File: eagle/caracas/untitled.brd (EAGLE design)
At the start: 110.2 x 53.3 mm, 26 parts, among them IC1 4027N, Q1 IRLZ44Z, X1 22-23-2021, X2 22-23-2021, X3 22-23-2041, X4 22-23-2041, X5 22-23-2021, X6 22-23-2021

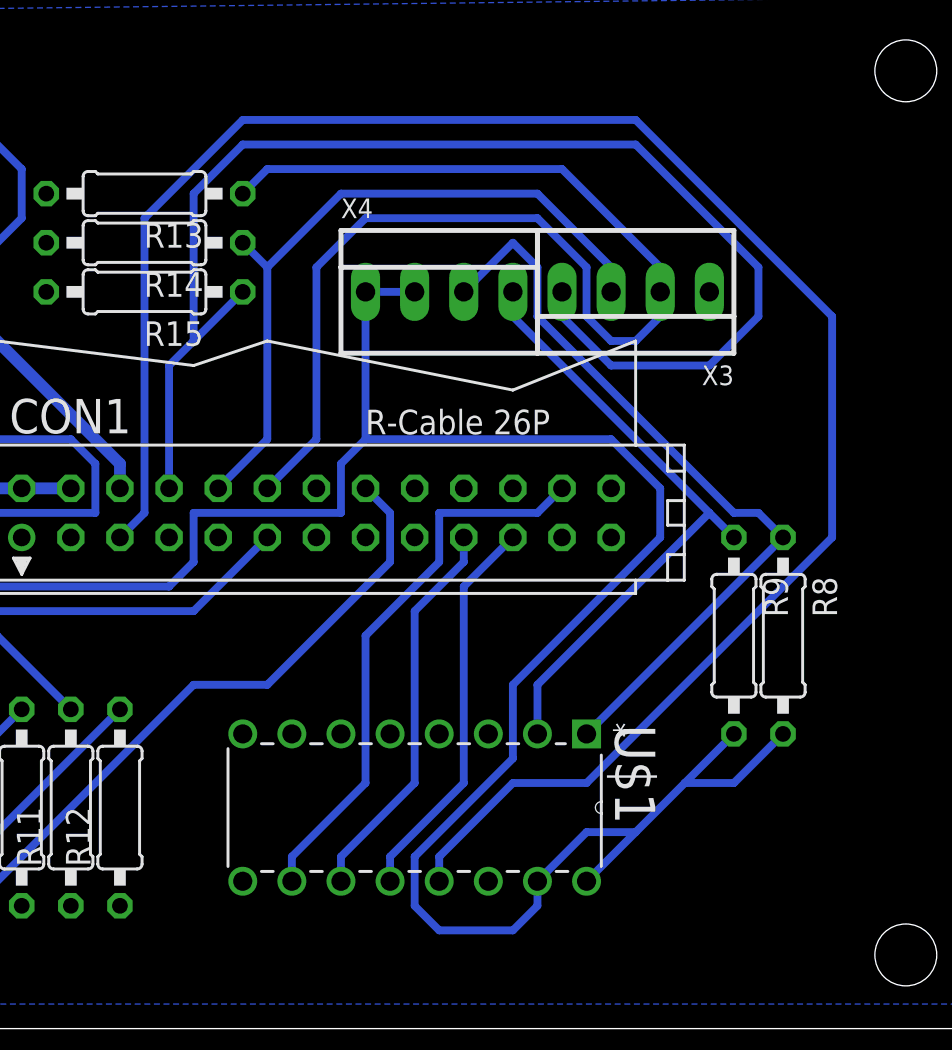
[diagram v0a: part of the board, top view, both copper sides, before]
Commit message: SPI clock in on pin 23, not pin 5
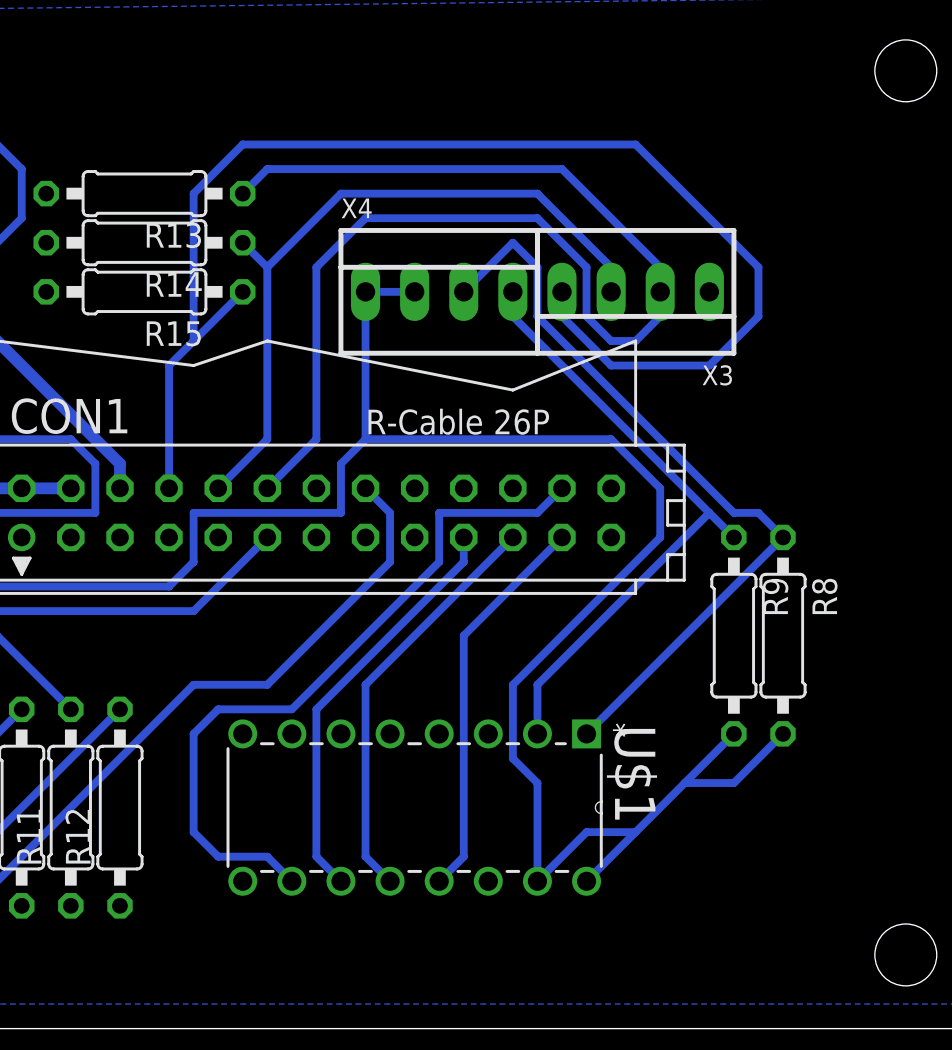
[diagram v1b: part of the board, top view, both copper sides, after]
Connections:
- net N$3: now also CON1.23; no longer CON1.5
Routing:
- net N$3: track 98.8 -> 20.4 mm
- net +3.3V: track 144.9 -> 133.4 mm
- net N$6: track 29.1 -> 37.0 mm
- net N$4: track 20.4 -> 21.5 mm
- net N$5: track 20.4 -> 21.5 mm
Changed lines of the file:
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@@
 <wire x1="59.69" y1="22.86" x2="68.58" y2="22.86" width="0.4064" layer="16"/>
 <wire x1="57.15" y1="25.4" x2="59.69" y2="22.86" width="0.4064" layer="16"/>
-<wire x1="87.63" y1="6.35" x2="87.63" y2="7.62" width="0.4064" layer="16"/>
-<wire x1="86.36" y1="5.08" x2="87.63" y2="6.35" width="0.4064" layer="16"/>
-<wire x1="82.55" y1="5.08" x2="86.36" y2="5.08" width="0.4064" layer="16"/>
-<wire x1="81.28" y1="6.35" x2="82.55" y2="5.08" width="0.4064" layer="16"/>
-<wire x1="81.28" y1="8.89" x2="81.28" y2="6.35" width="0.4064" layer="16"/>
-<wire x1="86.36" y1="13.97" x2="81.28" y2="8.89" width="0.4064" layer="16"/>
 <wire x1="86.36" y1="17.78" x2="86.36" y2="13.97" width="0.4064" layer="16"/>
 <wire x1="93.98" y1="25.4" x2="86.36" y2="17.78" width="0.4064" layer="16"/>
@@
 <wire x1="91.44" y1="30.48" x2="93.98" y2="27.94" width="0.4064" layer="16"/>
 <wire x1="78.74" y1="30.48" x2="91.44" y2="30.48" width="0.4064" layer="16"/>
+<wire x1="86.36" y1="13.97" x2="87.63" y2="12.7" width="0.4064" layer="16"/>
+<wire x1="87.63" y1="12.7" x2="87.63" y2="7.62" width="0.4064" layer="16"/>
 </signal>
 <signal name="+3.3V1">
@@
 <wire x1="57.15" y1="41.91" x2="55.88" y2="41.91" width="0.6096" layer="16"/>
 </signal>
-<signal name="N$3">
-<contactref element="CON1" pad="5"/>
-<contactref element="U$1" pad="13"/>
-<wire x1="67.31" y1="26.67" x2="66.04" y2="25.4" width="0.4064" layer="16"/>
-<wire x1="67.31" y1="41.91" x2="67.31" y2="26.67" width="0.4064" layer="16"/>
-<wire x1="72.39" y1="46.99" x2="67.31" y2="41.91" width="0.4064" layer="16"/>
-<wire x1="92.71" y1="46.99" x2="72.39" y2="46.99" width="0.4064" layer="16"/>
-<wire x1="102.87" y1="36.83" x2="92.71" y2="46.99" width="0.4064" layer="16"/>
-<wire x1="82.55" y1="7.62" x2="82.55" y2="8.89" width="0.4064" layer="16"/>
-<wire x1="82.55" y1="8.89" x2="86.36" y2="12.7" width="0.4064" layer="16"/>
-<wire x1="86.36" y1="12.7" x2="90.17" y2="12.7" width="0.4064" layer="16"/>
-<wire x1="102.87" y1="25.4" x2="102.87" y2="36.83" width="0.4064" layer="16"/>
-<wire x1="90.17" y1="12.7" x2="102.87" y2="25.4" width="0.4064" layer="16"/>
-</signal>
 <signal name="N$4">
 <contactref element="CON1" pad="21"/>
 <contactref element="U$1" pad="12"/>
-<wire x1="83.82" y1="22.86" x2="86.36" y2="25.4" width="0.4064" layer="16"/>
-<wire x1="83.82" y1="12.7" x2="83.82" y2="22.86" width="0.4064" layer="16"/>
-<wire x1="80.01" y1="8.89" x2="83.82" y2="12.7" width="0.4064" layer="16"/>
-<wire x1="80.01" y1="7.62" x2="80.01" y2="8.89" width="0.4064" layer="16"/>
+<wire x1="86.36" y1="25.4" x2="78.74" y2="17.78" width="0.4064" layer="16"/>
+<wire x1="78.74" y1="17.78" x2="78.74" y2="8.89" width="0.4064" layer="16"/>
+<wire x1="78.74" y1="8.89" x2="80.01" y2="7.62" width="0.4064" layer="16"/>
 </signal>
 <signal name="N$5">
@@
 <contactref element="U$1" pad="11"/>
 <wire x1="83.82" y1="24.13" x2="83.82" y2="25.4" width="0.4064" layer="16"/>
-<wire x1="81.28" y1="21.59" x2="83.82" y2="24.13" width="0.4064" layer="16"/>
-<wire x1="81.28" y1="12.7" x2="81.28" y2="21.59" width="0.4064" layer="16"/>
-<wire x1="77.47" y1="8.89" x2="81.28" y2="12.7" width="0.4064" layer="16"/>
-<wire x1="77.47" y1="7.62" x2="77.47" y2="8.89" width="0.4064" layer="16"/>
+<wire x1="83.82" y1="24.13" x2="76.2" y2="16.51" width="0.4064" layer="16"/>
+<wire x1="76.2" y1="16.51" x2="76.2" y2="8.89" width="0.4064" layer="16"/>
+<wire x1="76.2" y1="8.89" x2="77.47" y2="7.62" width="0.4064" layer="16"/>
 </signal>
 <signal name="N$6">
@@
 <wire x1="82.55" y1="26.67" x2="87.63" y2="26.67" width="0.4064" layer="16"/>
 <wire x1="82.55" y1="24.13" x2="82.55" y2="26.67" width="0.4064" layer="16"/>
-<wire x1="78.74" y1="20.32" x2="82.55" y2="24.13" width="0.4064" layer="16"/>
-<wire x1="78.74" y1="12.7" x2="78.74" y2="20.32" width="0.4064" layer="16"/>
-<wire x1="74.93" y1="8.89" x2="78.74" y2="12.7" width="0.4064" layer="16"/>
-<wire x1="74.93" y1="7.62" x2="74.93" y2="8.89" width="0.4064" layer="16"/>
+<wire x1="74.93" y1="7.62" x2="74.93" y2="8.89" width="0" layer="19" extent="1-16"/>
+<wire x1="82.55" y1="24.13" x2="74.93" y2="16.51" width="0.4064" layer="16"/>
+<wire x1="74.93" y1="16.51" x2="71.12" y2="16.51" width="0.4064" layer="16"/>
+<wire x1="71.12" y1="16.51" x2="69.85" y2="15.24" width="0.4064" layer="16"/>
+<wire x1="69.85" y1="15.24" x2="69.85" y2="10.16" width="0.4064" layer="16"/>
+<wire x1="69.85" y1="10.16" x2="71.12" y2="8.89" width="0.4064" layer="16"/>
+<wire x1="71.12" y1="8.89" x2="73.66" y2="8.89" width="0.4064" layer="16"/>
+<wire x1="73.66" y1="8.89" x2="74.93" y2="7.62" width="0.4064" layer="16"/>
 </signal>
 <signal name="N$9">
@@
 <wire x1="53.34" y1="22.86" x2="52.07" y2="22.86" width="0.4064" layer="16"/>
 </signal>
+<signal name="N$3">
+<contactref element="U$1" pad="13"/>
+<contactref element="CON1" pad="23"/>
+<wire x1="88.9" y1="25.4" x2="83.82" y2="20.32" width="0.4064" layer="16"/>
+<wire x1="83.82" y1="20.32" x2="83.82" y2="8.89" width="0.4064" layer="16"/>
+<wire x1="83.82" y1="8.89" x2="82.55" y2="7.62" width="0.4064" layer="16"/>
+</signal>
 </signals>

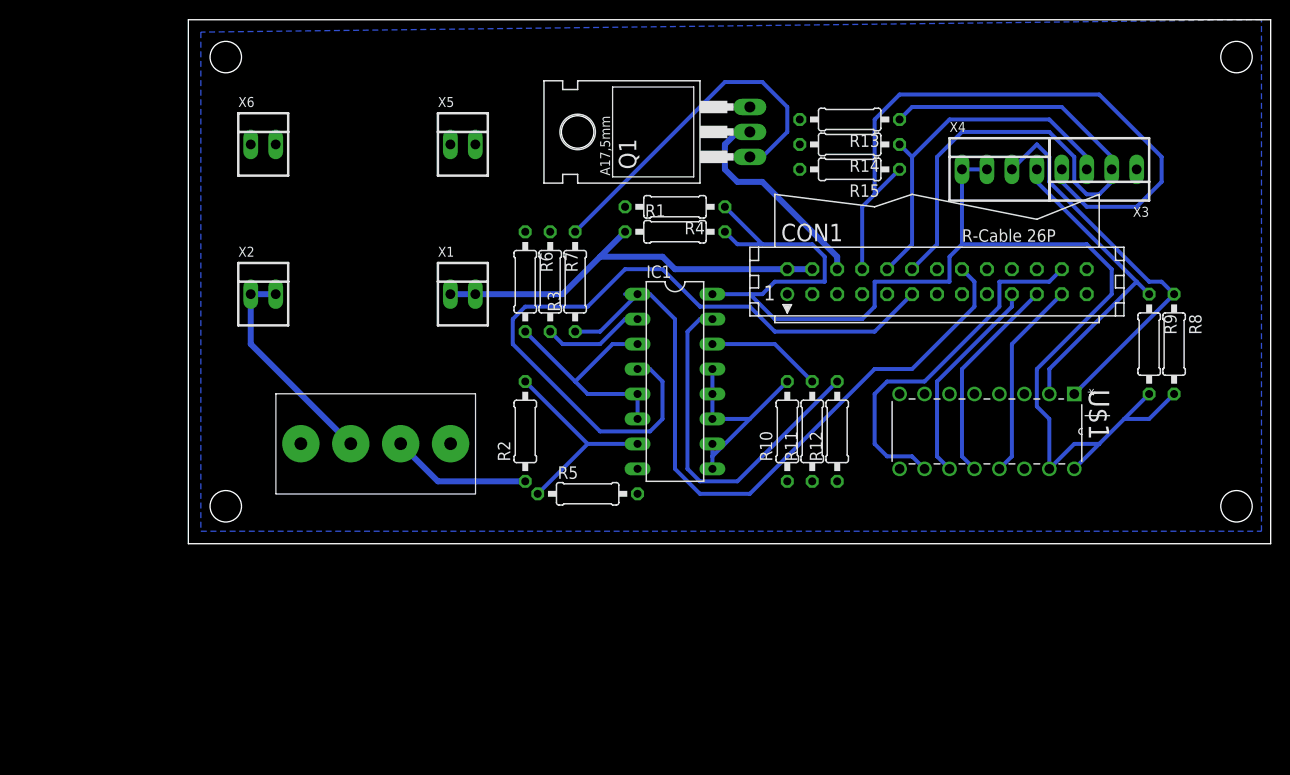
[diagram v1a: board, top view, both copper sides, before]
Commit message: Fixed errors in the electrical diagram.
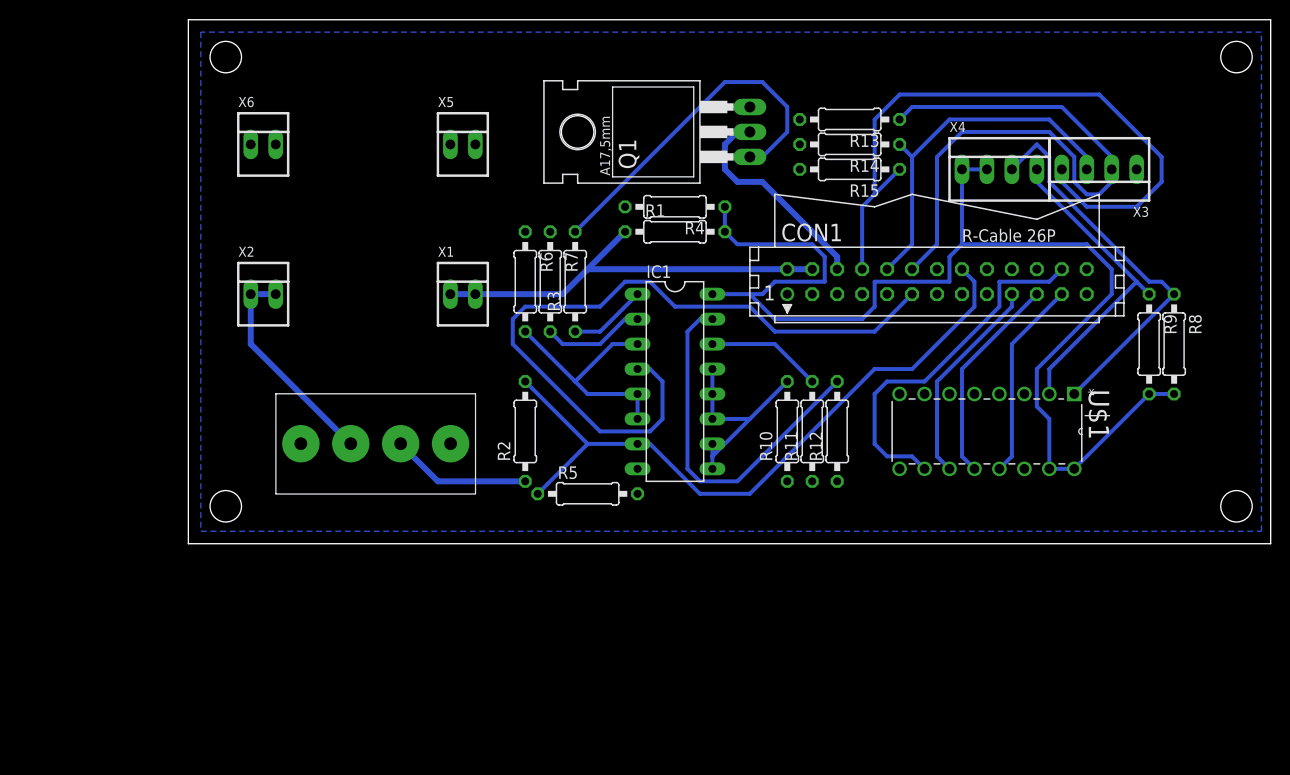
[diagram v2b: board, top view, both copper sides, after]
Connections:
- removed net +3.3V1: IC1.7, R2.2, R5.1
- new net N$14: IC1.1, R3.1
- net POWER_STATE: now also IC1.7, R2.2, R5.1; no longer IC1.1, R3.1
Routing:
- net +3.3V1: track 21.2 -> 0.00 mm
- net +3.3V: track 133.4 -> 123.3 mm
- net N$14: track 0.00 -> 7.93 mm
- net POWER_STATE: track 73.1 -> 69.9 mm
- net SUICIDE: track 75.8 -> 74.8 mm
- net +5V: track 42.5 -> 43.3 mm
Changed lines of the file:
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@@
 <vertex x="1.27" y="1.27"/>
 <vertex x="109.22" y="1.27"/>
-<vertex x="109.22" y="53.34"/>
+<vertex x="109.22" y="52.07"/>
 </polygon>
 <contactref element="Q1" pad="S"/>
 </signal>
 <signal name="POWER_STATE">
-<contactref element="IC1" pad="1"/>
-<contactref element="R3" pad="1"/>
 <contactref element="CON1" pad="16"/>
-<wire x1="45.72" y1="25.4" x2="44.45" y2="25.4" width="0.4064" layer="16"/>
 <wire x1="80.01" y1="26.67" x2="78.74" y2="27.94" width="0.4064" layer="16"/>
 <wire x1="80.01" y1="24.13" x2="80.01" y2="26.67" width="0.4064" layer="16"/>
@@
 <wire x1="57.15" y1="5.08" x2="69.85" y2="17.78" width="0.4064" layer="16"/>
 <wire x1="52.07" y1="5.08" x2="57.15" y2="5.08" width="0.4064" layer="16"/>
-<wire x1="49.53" y1="7.62" x2="52.07" y2="5.08" width="0.4064" layer="16"/>
-<wire x1="49.53" y1="22.86" x2="49.53" y2="7.62" width="0.4064" layer="16"/>
-<wire x1="46.99" y1="25.4" x2="49.53" y2="22.86" width="0.4064" layer="16"/>
-<wire x1="45.72" y1="25.4" x2="46.99" y2="25.4" width="0.4064" layer="16"/>
-<wire x1="39.37" y1="21.59" x2="41.91" y2="21.59" width="0.4064" layer="16"/>
-<wire x1="41.91" y1="21.59" x2="45.72" y2="25.4" width="0.4064" layer="16"/>
+<contactref element="IC1" pad="7"/>
+<contactref element="R2" pad="2"/>
+<contactref element="R5" pad="1"/>
+<wire x1="40.64" y1="10.16" x2="35.56" y2="5.08" width="0.4064" layer="16"/>
+<wire x1="40.64" y1="10.16" x2="34.29" y2="16.51" width="0.4064" layer="16"/>
+<wire x1="40.64" y1="10.16" x2="45.72" y2="10.16" width="0.4064" layer="16"/>
+<wire x1="45.72" y1="10.16" x2="46.99" y2="10.16" width="0.4064" layer="16"/>
+<wire x1="46.99" y1="10.16" x2="52.07" y2="5.08" width="0.4064" layer="16"/>
 </signal>
 <signal name="+12V_IGN" class="2">
@@
 <contactref element="X1" pad="2"/>
 <wire x1="63.5" y1="27.94" x2="60.96" y2="27.94" width="0.6096" layer="16"/>
-<wire x1="38.1" y1="25.4" x2="41.91" y2="29.21" width="0.6096" layer="16"/>
-<wire x1="41.91" y1="29.21" x2="44.45" y2="31.75" width="0.6096" layer="16"/>
+<wire x1="38.1" y1="25.4" x2="40.64" y2="27.94" width="0.6096" layer="16"/>
+<wire x1="40.64" y1="27.94" x2="44.45" y2="31.75" width="0.6096" layer="16"/>
 <wire x1="29.21" y1="25.4" x2="38.1" y2="25.4" width="0.6096" layer="16"/>
 <wire x1="29.21" y1="25.4" x2="26.67" y2="25.4" width="0.6096" layer="16"/>
-<wire x1="49.53" y1="27.94" x2="60.96" y2="27.94" width="0.6096" layer="16"/>
-<wire x1="48.26" y1="29.21" x2="49.53" y2="27.94" width="0.6096" layer="16"/>
-<wire x1="41.91" y1="29.21" x2="48.26" y2="29.21" width="0.6096" layer="16"/>
+<wire x1="40.64" y1="27.94" x2="60.96" y2="27.94" width="0.6096" layer="16"/>
 </signal>
 <signal name="+3.3V">
@@
 <contactref element="X4" pad="1"/>
 <contactref element="X4" pad="2"/>
-<wire x1="90.17" y1="7.62" x2="92.71" y2="10.16" width="0.4064" layer="16"/>
-<wire x1="92.71" y1="10.16" x2="95.25" y2="12.7" width="0.4064" layer="16"/>
-<wire x1="95.25" y1="12.7" x2="97.79" y2="15.24" width="0.4064" layer="16"/>
-<wire x1="97.79" y1="12.7" x2="100.33" y2="15.24" width="0.4064" layer="16"/>
-<wire x1="95.25" y1="12.7" x2="97.79" y2="12.7" width="0.4064" layer="16"/>
-<wire x1="90.17" y1="10.16" x2="87.63" y2="7.62" width="0.4064" layer="16"/>
-<wire x1="92.71" y1="10.16" x2="90.17" y2="10.16" width="0.4064" layer="16"/>
+<wire x1="90.17" y1="7.62" x2="97.79" y2="15.24" width="0.4064" layer="16"/>
 <wire x1="81.28" y1="38.1" x2="78.74" y2="38.1" width="0.4064" layer="16"/>
 <wire x1="58.42" y1="25.4" x2="57.15" y2="25.4" width="0.4064" layer="16"/>
@@
 <wire x1="64.77" y1="29.21" x2="64.77" y2="26.67" width="0.4064" layer="16"/>
 <wire x1="63.5" y1="30.48" x2="64.77" y2="29.21" width="0.4064" layer="16"/>
-<wire x1="55.88" y1="30.48" x2="58.42" y2="30.48" width="0.4064" layer="16"/>
-<wire x1="58.42" y1="30.48" x2="63.5" y2="30.48" width="0.4064" layer="16"/>
+<wire x1="55.88" y1="30.48" x2="63.5" y2="30.48" width="0.4064" layer="16"/>
 <wire x1="54.61" y1="31.75" x2="55.88" y2="30.48" width="0.4064" layer="16"/>
-<wire x1="58.42" y1="30.48" x2="54.61" y2="34.29" width="0.4064" layer="16"/>
 <wire x1="78.74" y1="30.48" x2="78.74" y2="38.1" width="0.4064" layer="16"/>
 <wire x1="77.47" y1="29.21" x2="78.74" y2="30.48" width="0.4064" layer="16"/>
@@
 <wire x1="86.36" y1="13.97" x2="87.63" y2="12.7" width="0.4064" layer="16"/>
 <wire x1="87.63" y1="12.7" x2="87.63" y2="7.62" width="0.4064" layer="16"/>
-</signal>
-<signal name="+3.3V1">
-<contactref element="IC1" pad="7"/>
-<contactref element="R2" pad="2"/>
-<contactref element="R5" pad="1"/>
-<wire x1="40.64" y1="10.16" x2="35.56" y2="5.08" width="0.4064" layer="16"/>
-<wire x1="45.72" y1="10.16" x2="40.64" y2="10.16" width="0.4064" layer="16"/>
-<wire x1="40.64" y1="10.16" x2="34.29" y2="16.51" width="0.4064" layer="16"/>
+<wire x1="87.63" y1="7.62" x2="90.17" y2="7.62" width="0.4064" layer="16"/>
+<wire x1="97.79" y1="15.24" x2="100.33" y2="15.24" width="0.4064" layer="16"/>
+<wire x1="54.61" y1="31.75" x2="54.61" y2="34.29" width="0.4064" layer="16"/>
 </signal>
 <signal name="N$1">
@@
 <wire x1="82.55" y1="26.67" x2="87.63" y2="26.67" width="0.4064" layer="16"/>
 <wire x1="82.55" y1="24.13" x2="82.55" y2="26.67" width="0.4064" layer="16"/>
-<wire x1="74.93" y1="7.62" x2="74.93" y2="8.89" width="0" layer="19" extent="1-16"/>
 <wire x1="82.55" y1="24.13" x2="74.93" y2="16.51" width="0.4064" layer="16"/>
 <wire x1="74.93" y1="16.51" x2="71.12" y2="16.51" width="0.4064" layer="16"/>
@@
 <wire x1="33.02" y1="22.86" x2="33.02" y2="20.32" width="0.4064" layer="16"/>
 <wire x1="34.29" y1="24.13" x2="33.02" y2="22.86" width="0.4064" layer="16"/>
-<wire x1="40.64" y1="24.13" x2="34.29" y2="24.13" width="0.4064" layer="16"/>
-<wire x1="44.45" y1="27.94" x2="40.64" y2="24.13" width="0.4064" layer="16"/>
-<wire x1="48.26" y1="27.94" x2="44.45" y2="27.94" width="0.4064" layer="16"/>
-<wire x1="52.07" y1="24.13" x2="48.26" y2="27.94" width="0.4064" layer="16"/>
-<wire x1="57.15" y1="24.13" x2="52.07" y2="24.13" width="0.4064" layer="16"/>
+<wire x1="41.91" y1="24.13" x2="34.29" y2="24.13" width="0.4064" layer="16"/>
+<wire x1="57.15" y1="24.13" x2="49.53" y2="24.13" width="0.4064" layer="16"/>
 <wire x1="59.69" y1="21.59" x2="57.15" y2="24.13" width="0.4064" layer="16"/>
 <wire x1="69.85" y1="21.59" x2="59.69" y2="21.59" width="0.4064" layer="16"/>
 <wire x1="73.66" y1="25.4" x2="69.85" y2="21.59" width="0.4064" layer="16"/>
+<wire x1="41.91" y1="24.13" x2="44.45" y2="26.67" width="0.4064" layer="16"/>
+<wire x1="44.45" y1="26.67" x2="46.99" y2="26.67" width="0.4064" layer="16"/>
+<wire x1="46.99" y1="26.67" x2="49.53" y2="24.13" width="0.4064" layer="16"/>
 </signal>
 <signal name="N$7">
@@
 <wire x1="83.82" y1="8.89" x2="82.55" y2="7.62" width="0.4064" layer="16"/>
 </signal>
+<signal name="N$14">
+<contactref element="IC1" pad="1"/>
+<contactref element="R3" pad="1"/>
+<wire x1="39.37" y1="21.59" x2="41.91" y2="21.59" width="0.4064" layer="16"/>
+<wire x1="41.91" y1="21.59" x2="45.72" y2="25.4" width="0.4064" layer="16"/>
+</signal>
 </signals>
